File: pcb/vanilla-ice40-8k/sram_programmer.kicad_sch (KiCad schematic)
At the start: 40 parts, among them J3 Conn_01x06_Pin, J4 Conn_01x02_Pin, U2 93LCxxBxxOT, U3 FT2232HL, U4 W25X40CLSN, Y1 12Mhz/18pf

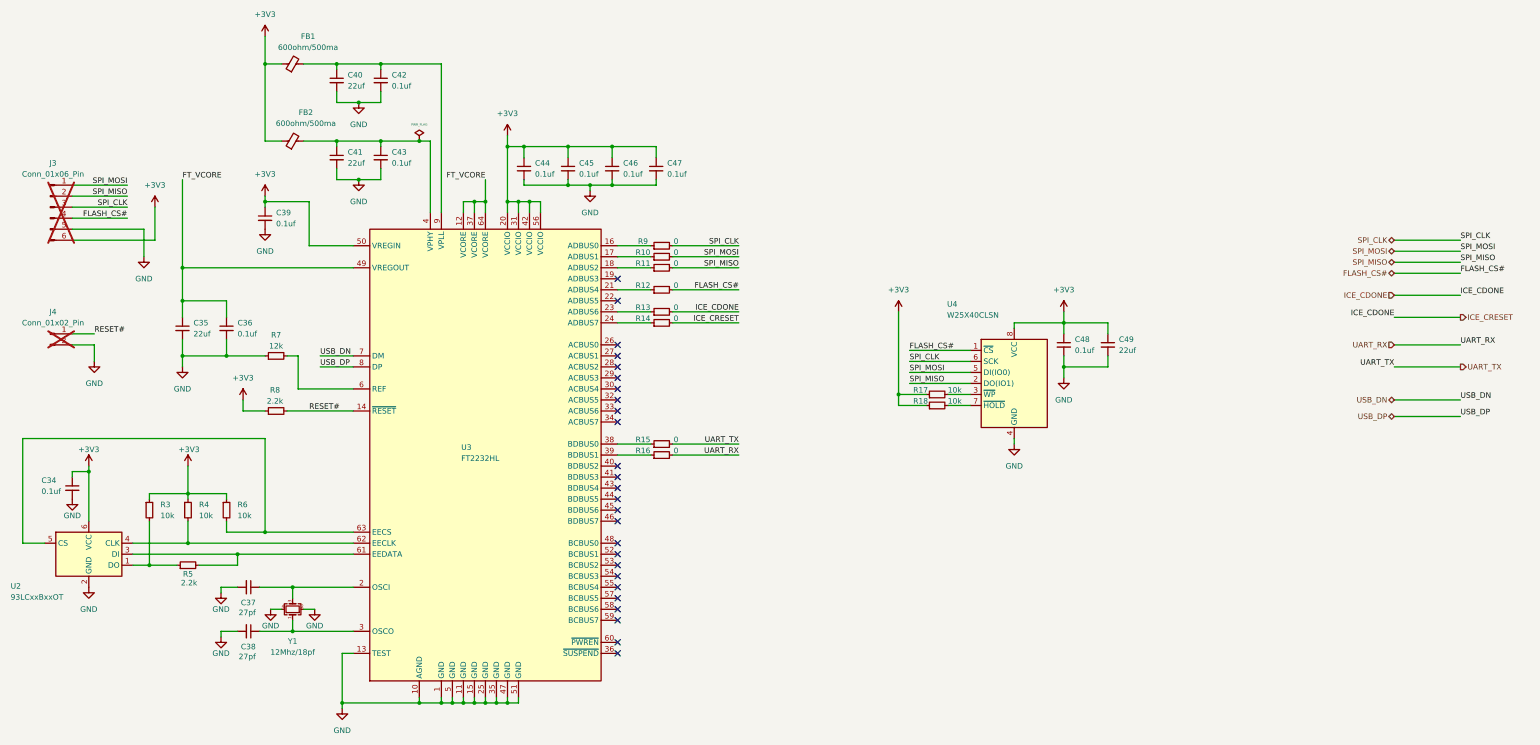
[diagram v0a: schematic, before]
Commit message: [pcb][hx8k] redid components with vip
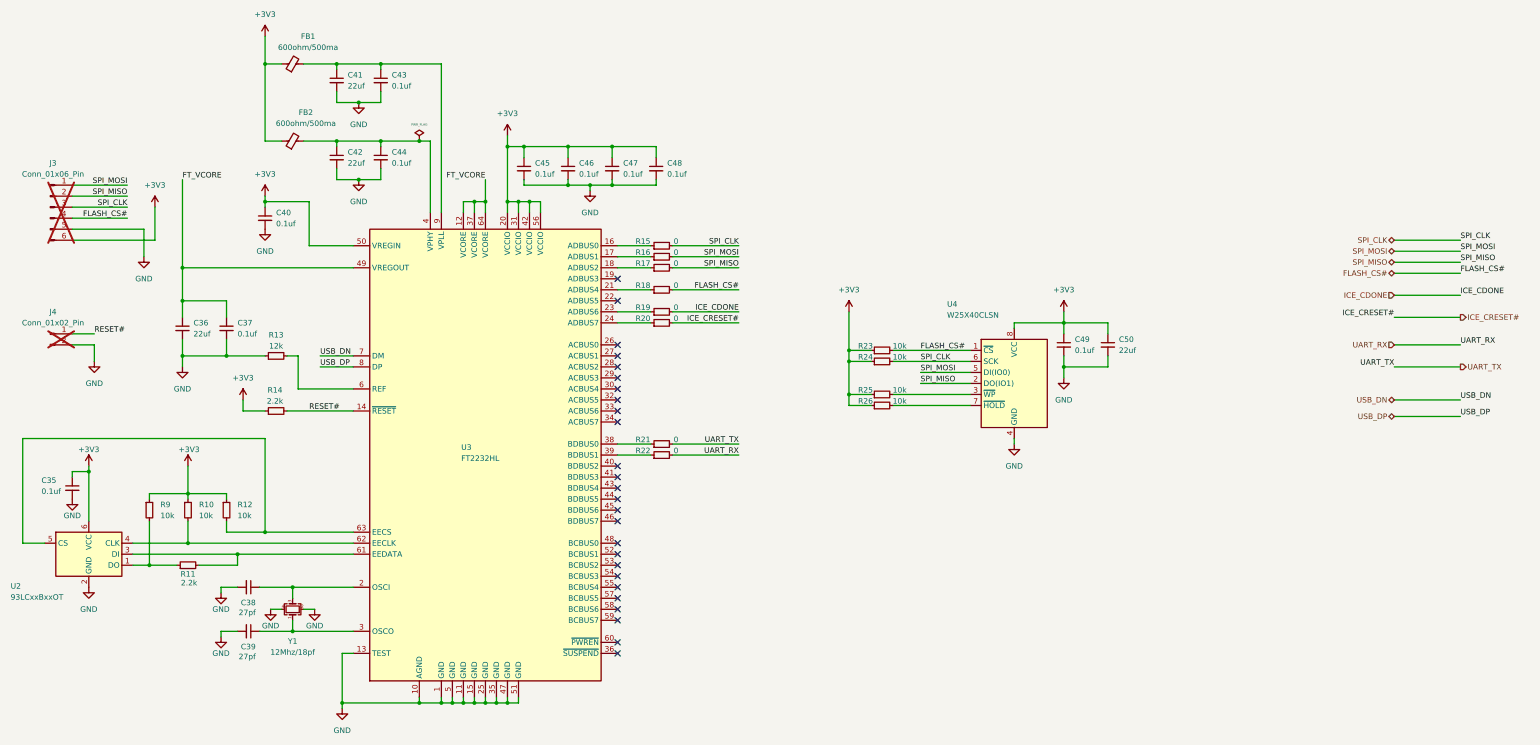
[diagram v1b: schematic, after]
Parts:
- added R23, R24: 10k, Resistor_SMD:R_0603_1608Metric, symbol Device:R_Small
- renumbered C34 to C35, C35 to C36, C36 to C37, C37 to C38, C38 to C39, C39 to C40, C40 to C41, C41 to C42, C42 to C43, C43 to C44, C44 to C45, C45 to C46, C46 to C47, C47 to C48, C48 to C49, C49 to C50, R4 to R10, R5 to R11, R6 to R12, R7 to R13, R8 to R14, R9 to R15, R10 to R16, R11 to R17, R12 to R18, R13 to R19, R14 to R20, R15 to R21, R16 to R22, R17 to R25, R18 to R26, R3 to R9
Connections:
- net +3V3: now also R23.1, R24.1
- net FLASH_CS#: now also R23.2
- net ICE_CDONE: no longer R20.2
- net SPI_CLK: now also R24.2
- new net ICE_CRESET#: R20.2
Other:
- moved on the sheet: R25, R26

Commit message: [pcb][hx8k] rerouted; all pins done
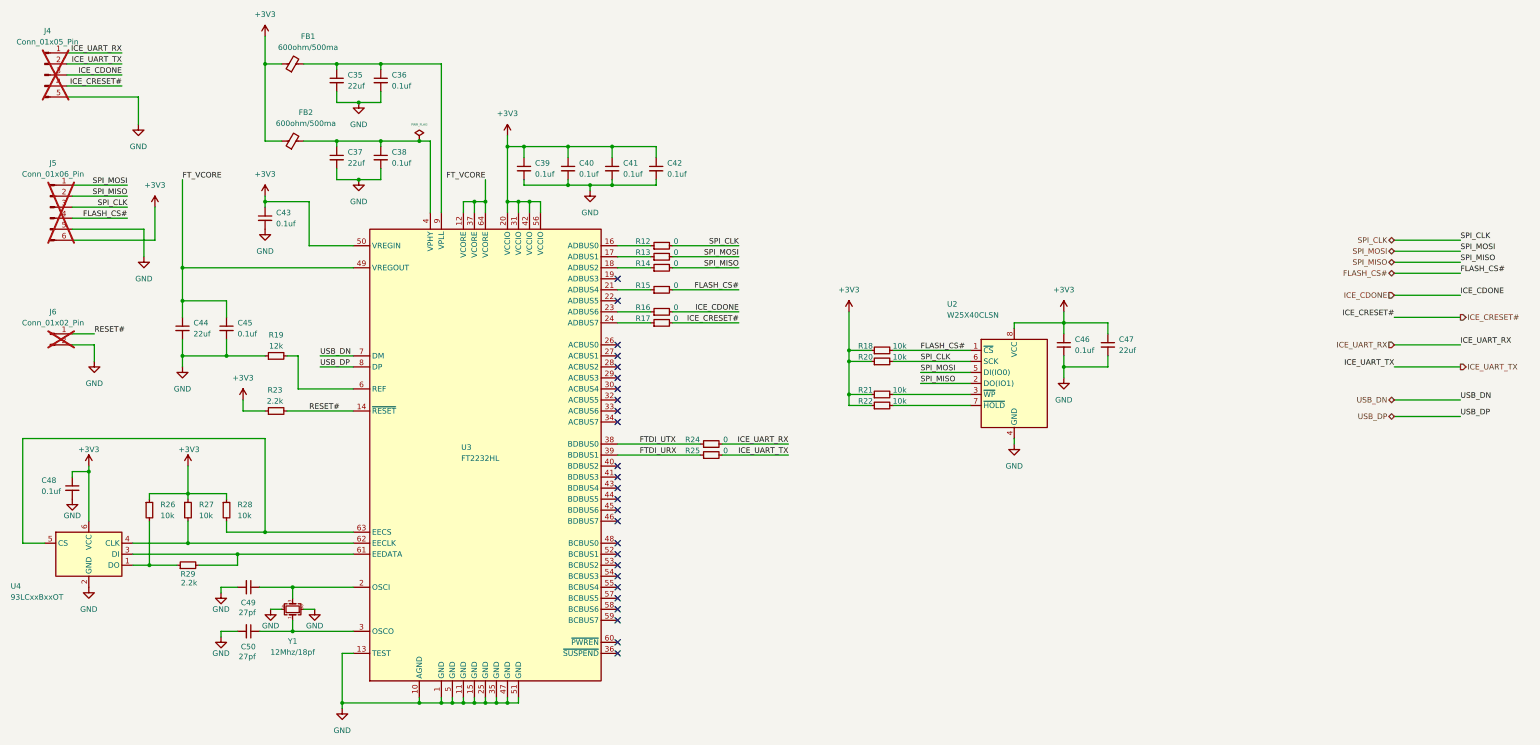
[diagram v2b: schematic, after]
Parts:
- added J4: Conn_01x05_Pin, Connector_PinHeader_2.54mm:PinHeader_1x05_P2.54mm_Vertical, symbol Connector:Conn_01x05_Pin
- renumbered C41 to C35, C43 to C36, C42 to C37, C44 to C38, C45 to C39, C46 to C40, C47 to C41, C48 to C42, C40 to C43, C36 to C44, C37 to C45, C49 to C46, C50 to C47, C35 to C48, C38 to C49, C39 to C50, J3 to J5, J4 to J6, R15 to R12, R16 to R13, R17 to R14, R18 to R15, R19 to R16, R20 to R17, R23 to R18, R13 to R19, R24 to R20, R25 to R21, R26 to R22, R14 to R23, R21 to R24, R22 to R25, R9 to R26, R10 to R27, R12 to R28, R11 to R29, U4 to U2, U2 to U4
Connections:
- net GND: now also J4.5 (Pin_5)
- net ICE_CDONE: now also J4.3 (Pin_3)
- net ICE_CRESET#: now also J4.4 (Pin_4)
- net FTDI_UTX: now reaches R24.1, U3.38 (BDBUS0)
- net FTDI_URX: now reaches R25.1, U3.39 (BDBUS1)
- net UART_RX renamed ICE_UART_TX
- net ICE_UART_TX: now also J4.2 (Pin_2)
- net UART_TX renamed ICE_UART_RX
- net ICE_UART_RX: now also J4.1 (Pin_1)
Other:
- moved on the sheet: R24, R25

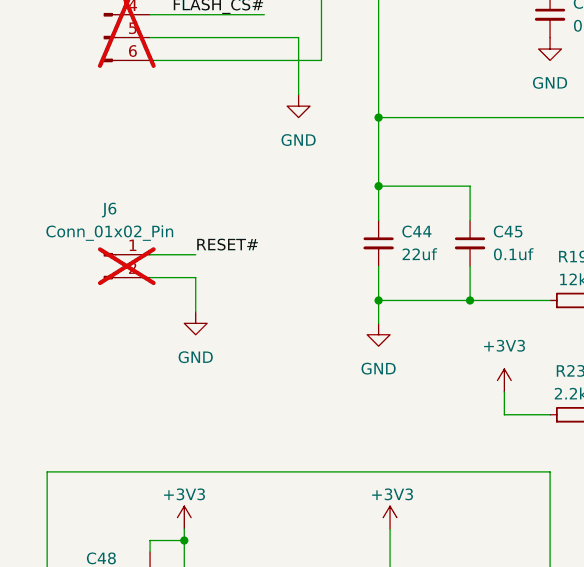
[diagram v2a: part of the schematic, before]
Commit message: [pcb][hx8k] added mounting holes
also changed ftdi disable to an unpopulated resistor
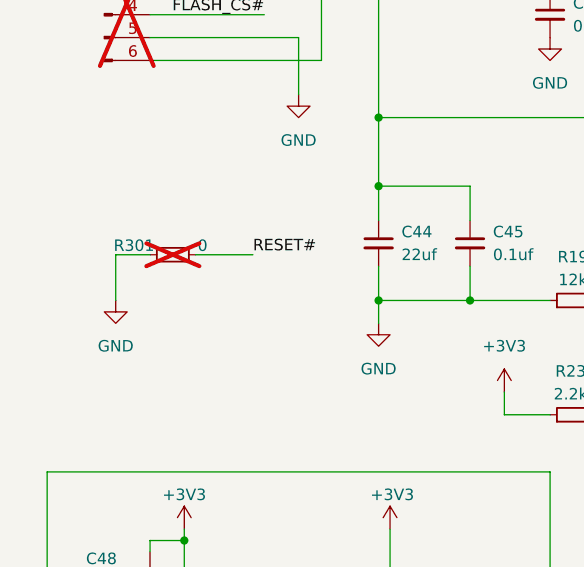
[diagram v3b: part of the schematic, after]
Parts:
- removed J6: Conn_01x02_Pin, Connector_PinHeader_2.54mm:PinHeader_1x02_P2.54mm_Vertical, symbol Connector:Conn_01x02_Pin
- added R301: 0, Resistor_SMD:R_0603_1608Metric, symbol Device:R_Small
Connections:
- net GND: now also R301.1
- net RESET#: now also R301.2
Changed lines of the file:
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@@
 	(wire
 		(pts
-			(xy 49.53 124.46) (xy 54.61 124.46)
+			(xy 38.1 170.18) (xy 43.18 170.18)
 		)
 		(stroke
@@
 	(wire
 		(pts
-			(xy 38.1 170.18) (xy 43.18 170.18)
+			(xy 288.29 127) (xy 288.29 129.54)
 		)
 		(stroke
@@
 	(wire
 		(pts
-			(xy 288.29 127) (xy 288.29 129.54)
+			(xy 64.77 67.31) (xy 64.77 73.66)
 		)
 		(stroke
@@
 	(wire
 		(pts
-			(xy 64.77 67.31) (xy 64.77 73.66)
+			(xy 49.53 121.92) (xy 45.72 121.92)
 		)
 		(stroke
@@
 	(wire
 		(pts
-			(xy 49.53 87.63) (xy 62.23 87.63)
+			(xy 45.72 121.92) (xy 45.72 127)
 		)
 		(stroke
@@
 	(wire
 		(pts
-			(xy 144.78 86.36) (xy 144.78 91.44)
+			(xy 49.53 87.63) (xy 62.23 87.63)
 		)
 		(stroke
@@
 	(wire
 		(pts
-			(xy 102.87 77.47) (xy 110.49 77.47)
+			(xy 144.78 86.36) (xy 144.78 91.44)
 		)
 		(stroke
@@
 	(wire
 		(pts
-			(xy 245.11 133.35) (xy 256.54 133.35)
+			(xy 102.87 77.47) (xy 110.49 77.47)
 		)
 		(stroke
@@
 	(wire
 		(pts
-			(xy 100.33 180.34) (xy 100.33 182.88)
+			(xy 245.11 133.35) (xy 256.54 133.35)
 		)
 		(stroke
@@
 	(wire
 		(pts
-			(xy 184.15 78.74) (xy 184.15 81.28)
+			(xy 100.33 180.34) (xy 100.33 182.88)
 		)
 		(stroke
@@
 	(wire
 		(pts
-			(xy 74.93 127) (xy 74.93 129.54)
+			(xy 184.15 78.74) (xy 184.15 81.28)
 		)
 		(stroke
@@
 	(wire
 		(pts
-			(xy 157.48 91.44) (xy 157.48 93.98)
+			(xy 74.93 127) (xy 74.93 129.54)
 		)
 		(stroke
@@
 	(wire
 		(pts
-			(xy 54.61 124.46) (xy 54.61 128.27)
+			(xy 157.48 91.44) (xy 157.48 93.98)
 		)
 		(stroke
@@
 	(wire
 		(pts
-			(xy 49.53 121.92) (xy 54.61 121.92)
-		)
-		(stroke
-			(width 0)
-			(type default)
-		)
-	)
-	(wire
-		(pts
 			(xy 184.15 86.36) (xy 184.15 87.63)
 		)
@@
 	(wire
 		(pts
+			(xy 54.61 121.92) (xy 60.96 121.92)
+		)
+		(stroke
+			(width 0)
+			(type default)
+		)
+	)
+	(wire
+		(pts
 			(xy 74.93 106.68) (xy 114.3 106.68)
 		)
@@
 	)
 	(label "RESET#"
-		(at 54.61 121.92 0)
+		(at 60.96 121.92 0)
 		(fields_autoplaced yes)
 		(effects
@@
 	(symbol
 		(lib_id "power:GND")
-		(at 54.61 128.27 0)
+		(at 45.72 127 0)
 		(unit 1)
 		(exclude_from_sim no)
@@
 		(fields_autoplaced yes)
 		(property "Reference" "#PWR052"
-			(at 54.61 134.62 0)
+			(at 45.72 133.35 0)
 			(effects
 				(font
@@
 		)
 		(property "Value" "GND"
-			(at 54.61 133.35 0)
+			(at 45.72 132.08 0)
 			(effects
 				(font
@@
 		)
 		(property "Footprint" ""
-			(at 54.61 128.27 0)
+			(at 45.72 127 0)
 			(effects
 				(font
@@
 		)
 		(property "Datasheet" ""
-			(at 54.61 128.27 0)
+			(at 45.72 127 0)
 			(effects
 				(font
@@
 		)
 		(property "Description" "Power symbol creates a global label with name \"GND\" , ground"
-			(at 54.61 128.27 0)
+			(at 45.72 127 0)
 			(effects
 				(font
@@
 	)
 	(symbol
+		(lib_id "Device:R_Small")
+		(at 52.07 121.92 90)
+		(unit 1)
+		(exclude_from_sim no)
+		(in_bom yes)
+		(on_board yes)
+		(dnp yes)
+		(property "Reference" "R301"
+			(at 47.752 120.904 90)
+			(effects
+				(font
+					(size 1.27 1.27)
+				)
+			)
+		)
+		(property "Value" "0"
+			(at 55.372 120.904 90)
+			(effects
+				(font
+					(size 1.27 1.27)
+				)
+			)
+		)
+		(property "Footprint" "Resistor_SMD:R_0603_1608Metric"
+			(at 52.07 121.92 0)
+			(effects
+				(font
+					(size 1.27 1.27)
+				)
+				(hide yes)
+			)
+		)
+		(property "Datasheet" "~"
+			(at 52.07 121.92 0)
+			(effects
+				(font
+					(size 1.27 1.27)
+				)
+				(hide yes)
+			)
+		)
+		(property "Description" "Resistor, small symbol"
+			(at 52.07 121.92 0)
+			(effects
+				(font
+					(size 1.27 1.27)
+				)
+				(hide yes)
+			)
+		)
+		(property "LCSC Part #" "C21189"
+			(at 52.07 121.92 0)
+			(effects
+				(font
+					(size 1.27 1.27)
+				)
+				(hide yes)
+			)
+		)
+		(property "JLCPCB Rotation Offset" ""
+			(at 52.07 121.92 0)
+			(effects
+				(font
+					(size 1.27 1.27)
+				)
+				(hide yes)
+			)
+		)
+		(property "Digi-Key Part Number" "CR0603-J/-000ELFCT-ND"
+			(at 52.07 121.92 0)
+			(effects
+				(font
+					(size 1.27 1.27)
+				)
+				(hide yes)
+			)
+		)
+		(pin "2"
+		)
+		(pin "1"
+		)
+		(instances
+			(project "vanilla-ice40-8k"
+				(path "/6fdfbf4b-014a-4077-8dc3-7ce5ecaf5fe5/8fcffd86-9b82-4947-9420-a56f34009c5e"
+					(reference "R301")
+					(unit 1)
+				)
+			)
+		)
+	)
+	(symbol
 		(lib_id "power:GND")
 		(at 168.91 88.9 0)
@@
 					(unit 1)
 				)
-			)
-		)
-	)
-	(symbol
-		(lib_id "Connector:Conn_01x02_Pin")
-		(at 44.45 121.92 0)
-		(unit 1)
-		(exclude_from_sim no)
-		(in_bom no)
-		(on_board yes)
-		(dnp yes)
-		(fields_autoplaced yes)
-		(property "Reference" "J6"
-			(at 45.085 116.84 0)
-			(effects
-				(font
-					(size 1.27 1.27)
-				)
-			)
-		)
-		(property "Value" "Conn_01x02_Pin"
-			(at 45.085 119.38 0)
-			(effects
-				(font
-					(size 1.27 1.27)
-				)
-			)
-		)
-		(property "Footprint" "Connector_PinHeader_2.54mm:PinHeader_1x02_P2.54mm_Vertical"
-			(at 44.45 121.92 0)
-			(effects
-				(font
-					(size 1.27 1.27)
-				)
-				(hide yes)
-			)
-		)
-		(property "Datasheet" "~"
-			(at 44.45 121.92 0)
-			(effects
-				(font
-					(size 1.27 1.27)
-				)
-				(hide yes)
-			)
-		)
-		(property "Description" "Generic connector, single row, 01x02, script generated"
-			(at 44.45 121.92 0)
-			(effects
-				(font
-					(size 1.27 1.27)
-				)
-				(hide yes)
-			)
-		)
-		(property "JLCPCB Rotation Offset" ""
-			(at 44.45 121.92 0)
-			(effects
-				(font
-					(size 1.27 1.27)
-				)
-				(hide yes)
-			)
-		)
-		(property "Digi-Key Part Number" ""
-			(at 44.45 121.92 0)
-			(effects
-				(font
-					(size 1.27 1.27)
-				)
-				(hide yes)
-			)
-		)
-		(pin "1"
-		)
-		(pin "2"
-		)
-		(instances
-			(project "vanilla-ice40-8k"
-				(path "/6fdfbf4b-014a-4077-8dc3-7ce5ecaf5fe5/8fcffd86-9b82-4947-9420-a56f34009c5e"
-					(reference "J6")
-					(unit 1)
-				)

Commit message: [pcb][hx8k] finalize for production
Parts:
- J4, J5: Digi-Key Part Number (none) -> DNP; LCSC Part # (none) -> DNP
- R301: now left out of the parts list
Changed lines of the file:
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@@
 			)
 		)
-		(property "Digi-Key Part Number" ""
+		(property "Digi-Key Part Number" "DNP"
+			(at 44.45 92.71 0)
+			(effects
+				(font
+					(size 1.27 1.27)
+				)
+				(hide yes)
+			)
+		)
+		(property "LCSC Part #" "DNP"
 			(at 44.45 92.71 0)
 			(effects
@@
 		(unit 1)
 		(exclude_from_sim no)
-		(in_bom yes)
+		(in_bom no)
 		(on_board yes)
 		(dnp yes)
@@
 			)
 		)
-		(property "Digi-Key Part Number" ""
+		(property "Digi-Key Part Number" "DNP"
 			(at 43.18 62.23 0)
 			(effects
+				(font
+					(size 1.27 1.27)
+				)
+				(hide yes)
+			)
+		)
+		(property "LCSC Part #" "DNP"
+			(at 43.18 62.23 0)
+			(effects

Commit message: [hx8k][pcb] place and route stackable connector on left
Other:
- title: (none) -> Vanilia Ice HX8K
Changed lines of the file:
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@@
 	(generator_version "8.0")
 	(paper "USLedger")
+	(title_block
+		(title "Vanilia Ice HX8K")
+		(rev "1.5.0")
+	)
 	(junction
 		(at 147.32 207.01)

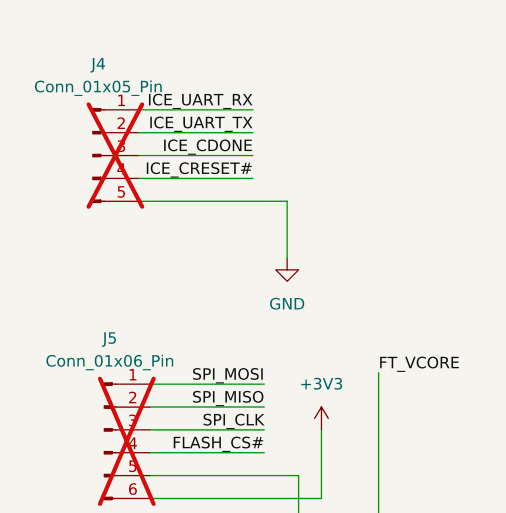
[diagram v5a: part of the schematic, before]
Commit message: [hx8k][pcb] updated J refs
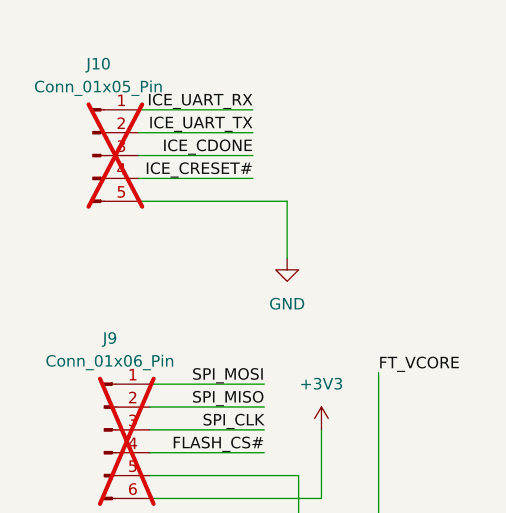
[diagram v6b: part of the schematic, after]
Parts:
- renumbered J4 to J10, J5 to J9
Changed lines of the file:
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@@
 		(dnp yes)
 		(fields_autoplaced yes)
-		(property "Reference" "J5"
+		(property "Reference" "J9"
 			(at 45.085 82.55 0)
 			(effects
@@
 			(project "vanilla-ice40-8k"
 				(path "/6fdfbf4b-014a-4077-8dc3-7ce5ecaf5fe5/8fcffd86-9b82-4947-9420-a56f34009c5e"
-					(reference "J5")
+					(reference "J9")
 					(unit 1)
 				)
@@
 		(dnp yes)
 		(fields_autoplaced yes)
-		(property "Reference" "J4"
+		(property "Reference" "J10"
 			(at 43.815 52.07 0)
 			(effects
@@
 			(project "vanilla-ice40-8k"
 				(path "/6fdfbf4b-014a-4077-8dc3-7ce5ecaf5fe5/8fcffd86-9b82-4947-9420-a56f34009c5e"
-					(reference "J4")
-					(unit 1)
-				)
+					(reference "J10")
+					(unit 1)
+				)
